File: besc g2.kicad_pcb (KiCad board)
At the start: 4 copper layers, 231 x 67 mm, 302 parts, among them IC1 LTC7801, J1 PHASE WIRE, J10 614105150721, J11 THROTTLE, J12 MOTOR SENSOR, J13 THROTTLE 2 (BRAKE), J14 SERIAL, J15 IGNITION, J16 CAN, J17 12V OUT, J2 PHASE WIRE, J3 PHASE WIRE, J4 BUSBAR, J5 BUSBAR, J6 IN+, J7 IN-, J8 SWD, J9 RC PWM, Q1 IRF135B203, Q10 IRF135B203, Q11 IRF135B203, Q12 IRF135B203, Q13 IRF135B203, Q14 IRF135B203, Q15 IRF135B203, Q16 IRF135B203, Q17 IRF135B203, Q18 IRF135B203, Q19 IRF135B203, Q2 IRF135B203, Q20 IRF135B203, Q21 IRF135B203, Q22 IRF135B203, Q23 IRF135B203, Q24 IRF135B203, Q25 FDMS86252L, Q26 BSC110N15NS5, Q3 IRF135B203, Q4 IRF135B203, Q5 IRF135B203, Q6 IRF135B203, Q7 IRF135B203, Q8 IRF135B203, Q9 IRF135B203, U1 UCC21520DW, U10 TJA1051T-3, U11 R-78E5.0-0.5, U12 LP5907MFX-3.3, U2 UCC21520DW, U3 UCC21520DW, U4 INA240A1D, U5 INA240A1D, U6 INA240A1D, U7 SN74LVC1G04, U8 STM32F405RGTx, U9 USBLC6-2SC6, Y1 MCSJK-7I-8.00-18-10-60-B-10

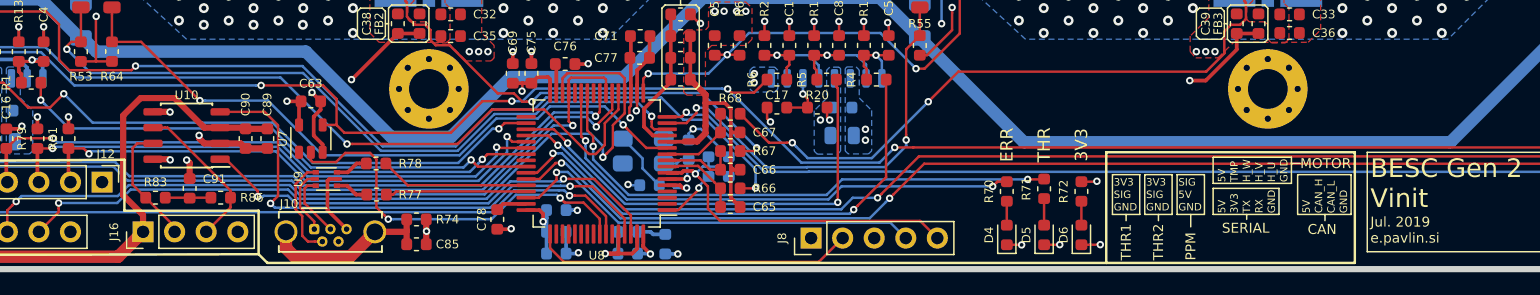
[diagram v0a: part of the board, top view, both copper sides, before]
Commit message: removed inverter for gate enable, fixed bugs on pcb
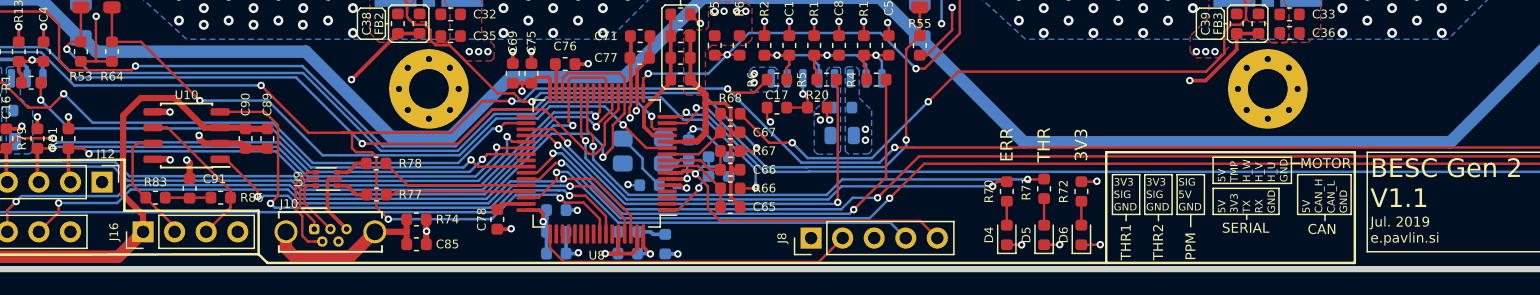
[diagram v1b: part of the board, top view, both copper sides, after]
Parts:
- removed C63: 100n, Capacitor_SMD:C_0603_1608Metric
- removed U7: SN74LVC1G04, Package_TO_SOT_SMD:SOT-23-5
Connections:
- U8 pad 57: /mcu/GATE_ENABLE -> /mcu/DISABLE
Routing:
- net /mcu/GATE_ENABLE: track 31.6 -> 0.00 mm, vias 2 -> 0
- net /mcu/DISABLE: track 156.3 -> 183.5 mm, vias 5 -> 7
- net GND: track 213.3 -> 207.6 mm, vias 242 -> 241
- net +3V3: track 121.3 -> 118.1 mm, vias 30 -> 29
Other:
- board text added: "BESC Gen 2 V1.1"
- board text removed: "BESC Gen 2 Vinit"
